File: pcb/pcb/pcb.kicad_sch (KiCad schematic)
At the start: 22 parts, among them J1 UART, J2 Barrel_Jack, J3 Stepper, SW1 RESET, SW2 FLASH, U1 ESP32-WROOM-32, U2 TSR_1-2433

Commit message: tweaks from reddit wiki
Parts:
- H1: footprint MountingHole:MountingHole_2.7mm_M2.5_Pad -> MountingHole:MountingHole_3.2mm_M3_DIN965_Pad
- H2, H3, H4: footprint MountingHole:MountingHole_2.5mm_Pad -> MountingHole:MountingHole_3.2mm_M3_DIN965_Pad
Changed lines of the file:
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@@
       (effects (font (size 1.27 1.27)) (justify left))
     )
-    (property "Footprint" "MountingHole:MountingHole_2.5mm_Pad" (id 2) (at 52.07 27.94 0)
+    (property "Footprint" "MountingHole:MountingHole_3.2mm_M3_DIN965_Pad" (id 2) (at 52.07 27.94 0)
       (effects (font (size 1.27 1.27)) hide)
     )
@@
       (effects (font (size 1.27 1.27)) (justify left))
     )
-    (property "Footprint" "MountingHole:MountingHole_2.7mm_M2.5_Pad" (id 2) (at 34.29 27.94 0)
+    (property "Footprint" "MountingHole:MountingHole_3.2mm_M3_DIN965_Pad" (id 2) (at 34.29 27.94 0)
       (effects (font (size 1.27 1.27)) hide)
     )
@@
       (effects (font (size 1.27 1.27)) (justify left))
     )
-    (property "Footprint" "MountingHole:MountingHole_2.5mm_Pad" (id 2) (at 69.85 27.94 0)
+    (property "Footprint" "MountingHole:MountingHole_3.2mm_M3_DIN965_Pad" (id 2) (at 69.85 27.94 0)
       (effects (font (size 1.27 1.27)) hide)
     )
@@
       (effects (font (size 1.27 1.27)) (justify left))
     )
-    (property "Footprint" "MountingHole:MountingHole_2.5mm_Pad" (id 2) (at 87.63 27.94 0)
+    (property "Footprint" "MountingHole:MountingHole_3.2mm_M3_DIN965_Pad" (id 2) (at 87.63 27.94 0)
       (effects (font (size 1.27 1.27)) hide)
     )
@@
     )
     (path "/34fa3d54-c535-425c-b022-e1943d8d5f86"
-      (reference "H1") (unit 1) (value "MountingHole") (footprint "MountingHole:MountingHole_2.7mm_M2.5_Pad")
+      (reference "H1") (unit 1) (value "MountingHole") (footprint "MountingHole:MountingHole_3.2mm_M3_DIN965_Pad")
     )
     (path "/00d9b647-6f7b-4061-b8f8-f07282eb45d6"
-      (reference "H2") (unit 1) (value "MountingHole") (footprint "MountingHole:MountingHole_2.5mm_Pad")
+      (reference "H2") (unit 1) (value "MountingHole") (footprint "MountingHole:MountingHole_3.2mm_M3_DIN965_Pad")
     )
     (path "/72d1a3aa-0e7b-4b10-a84c-7a0d93e80db5"
-      (reference "H3") (unit 1) (value "MountingHole") (footprint "MountingHole:MountingHole_2.5mm_Pad")
+      (reference "H3") (unit 1) (value "MountingHole") (footprint "MountingHole:MountingHole_3.2mm_M3_DIN965_Pad")
     )
     (path "/b3ffd185-6873-4234-b901-27672efba3ad"
-      (reference "H4") (unit 1) (value "MountingHole") (footprint "MountingHole:MountingHole_2.5mm_Pad")
+      (reference "H4") (unit 1) (value "MountingHole") (footprint "MountingHole:MountingHole_3.2mm_M3_DIN965_Pad")
     )
     (path "/f859e7d0-40bd-4ce3-9e1e-50d116474f0f"

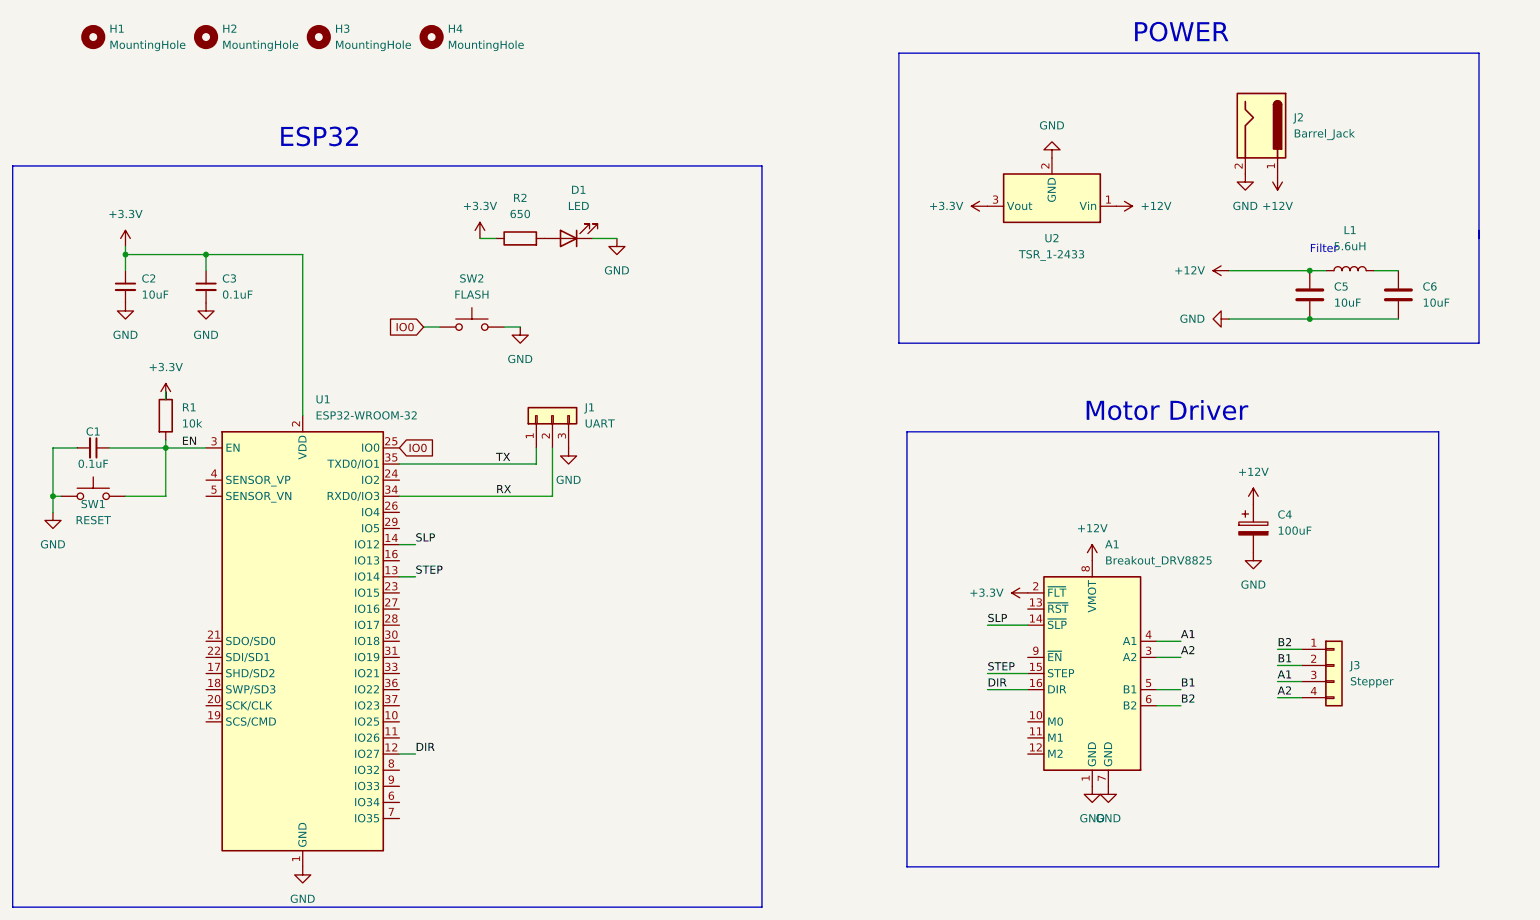
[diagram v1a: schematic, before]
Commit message: add activity led and general tidy
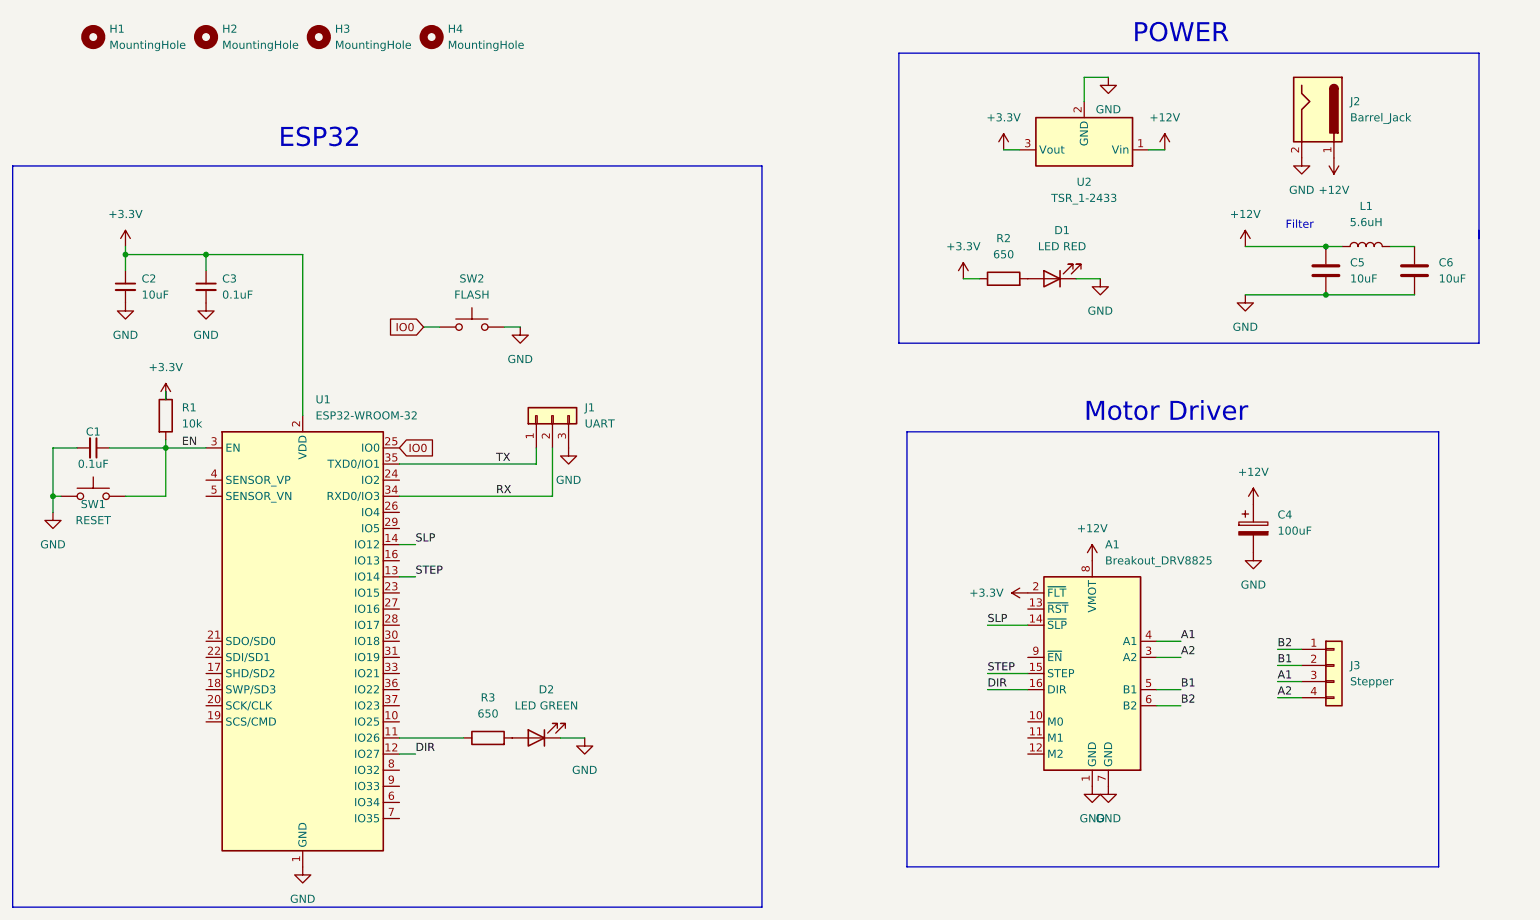
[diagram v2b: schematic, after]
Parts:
- added D2: LED GREEN, LED_SMD:LED_1206_3216Metric_Pad1.42x1.75mm_HandSolder, symbol Device:LED
- added R3: 650, Resistor_SMD:R_1206_3216Metric_Pad1.30x1.75mm_HandSolder, symbol Device:R
- D1: value LED -> LED RED
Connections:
- net GND: now also D2.1 (K)
- net at U1.11 (IO26): now also R3.1
- new net: D2.2 (A), R3.2
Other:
- moved on the sheet: C5, C6, D1, J2, L1, R2, U2

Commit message: general tweaks
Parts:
- H1, H2, H3, H4: footprint MountingHole:MountingHole_3.2mm_M3_DIN965_Pad -> MountingHole:MountingHole_3.2mm_M3_Pad
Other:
- title: (none) -> twilight
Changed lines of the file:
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@@
 (kicad_sch (version 20211123) (generator eeschema)
   (paper "A4")
+  (title_block
+    (title "twilight")
+    (date "2022-01-28")
+    (rev "1.0")
+    (comment 4 "ESP32 and DRV8825 based stepper motor controller")
+  )
   (junction (at 52.07 62.23) (diameter 0) (color 0 0 0 0)
   )
@@
   )
   (wire (pts (xy 104.14 92.71) (xy 104.14 95.25))
+    (stroke (width 0) (type default) (color 0 0 0 0))
+  )
+  (wire (pts (xy 179.07 115.57) (xy 181.61 115.57))
     (stroke (width 0) (type default) (color 0 0 0 0))
   )
@@
       (effects (font (size 1.27 1.27)) (justify left))
     )
-    (property "Footprint" "MountingHole:MountingHole_3.2mm_M3_DIN965_Pad" (id 2) (at 52.07 27.94 0)
+    (property "Footprint" "MountingHole:MountingHole_3.2mm_M3_Pad" (id 2) (at 52.07 27.94 0)
       (effects (font (size 1.27 1.27)) hide)
     )
@@
       (effects (font (size 1.27 1.27)) (justify left))
     )
-    (property "Footprint" "MountingHole:MountingHole_3.2mm_M3_DIN965_Pad" (id 2) (at 34.29 27.94 0)
+    (property "Footprint" "MountingHole:MountingHole_3.2mm_M3_Pad" (id 2) (at 34.29 27.94 0)
       (effects (font (size 1.27 1.27)) hide)
     )
@@
       (effects (font (size 1.27 1.27)) (justify left))
     )
-    (property "Footprint" "MountingHole:MountingHole_3.2mm_M3_DIN965_Pad" (id 2) (at 69.85 27.94 0)
+    (property "Footprint" "MountingHole:MountingHole_3.2mm_M3_Pad" (id 2) (at 69.85 27.94 0)
       (effects (font (size 1.27 1.27)) hide)
     )
@@
       (effects (font (size 1.27 1.27)) (justify left))
     )
-    (property "Footprint" "MountingHole:MountingHole_3.2mm_M3_DIN965_Pad" (id 2) (at 87.63 27.94 0)
+    (property "Footprint" "MountingHole:MountingHole_3.2mm_M3_Pad" (id 2) (at 87.63 27.94 0)
       (effects (font (size 1.27 1.27)) hide)
     )
@@
     (pin "1")
   )
-  (symbol (lib_id "power:+3.3V") (at 181.61 115.57 90) (unit 1)
-    (in_bom yes) (on_board yes) (fields_autoplaced)
-    (property "Reference" "#PWR09" (id 0) (at 185.42 115.57 0)
-      (effects (font (size 1.27 1.27)) hide)
-    )
-    (property "Value" "+3.3V" (id 1) (at 177.8 115.5699 90)
-      (effects (font (size 1.27 1.27)) (justify left))
-    )
-    (property "Footprint" "" (id 2) (at 181.61 115.57 0)
-      (effects (font (size 1.27 1.27)) hide)
-    )
-    (property "Datasheet" "" (id 3) (at 181.61 115.57 0)
+  (symbol (lib_id "power:+3.3V") (at 179.07 115.57 0) (unit 1)
+    (in_bom yes) (on_board yes) (fields_autoplaced)
+    (property "Reference" "#PWR09" (id 0) (at 179.07 119.38 0)
+      (effects (font (size 1.27 1.27)) hide)
+    )
+    (property "Value" "+3.3V" (id 1) (at 179.07 110.49 0))
+    (property "Footprint" "" (id 2) (at 179.07 115.57 0)
+      (effects (font (size 1.27 1.27)) hide)
+    )
+    (property "Datasheet" "" (id 3) (at 179.07 115.57 0)
       (effects (font (size 1.27 1.27)) hide)
     )
@@
     )
     (path "/34fa3d54-c535-425c-b022-e1943d8d5f86"
-      (reference "H1") (unit 1) (value "MountingHole") (footprint "MountingHole:MountingHole_3.2mm_M3_DIN965_Pad")
+      (reference "H1") (unit 1) (value "MountingHole") (footprint "MountingHole:MountingHole_3.2mm_M3_Pad")
     )
     (path "/00d9b647-6f7b-4061-b8f8-f07282eb45d6"
-      (reference "H2") (unit 1) (value "MountingHole") (footprint "MountingHole:MountingHole_3.2mm_M3_DIN965_Pad")
+      (reference "H2") (unit 1) (value "MountingHole") (footprint "MountingHole:MountingHole_3.2mm_M3_Pad")
     )
     (path "/72d1a3aa-0e7b-4b10-a84c-7a0d93e80db5"
-      (reference "H3") (unit 1) (value "MountingHole") (footprint "MountingHole:MountingHole_3.2mm_M3_DIN965_Pad")
+      (reference "H3") (unit 1) (value "MountingHole") (footprint "MountingHole:MountingHole_3.2mm_M3_Pad")
     )
     (path "/b3ffd185-6873-4234-b901-27672efba3ad"
-      (reference "H4") (unit 1) (value "MountingHole") (footprint "MountingHole:MountingHole_3.2mm_M3_DIN965_Pad")
+      (reference "H4") (unit 1) (value "MountingHole") (footprint "MountingHole:MountingHole_3.2mm_M3_Pad")
     )
     (path "/f859e7d0-40bd-4ce3-9e1e-50d116474f0f"

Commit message: tidy schematic
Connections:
- net +12V: no longer U2.1 (Vin)
- net A1: now also J3.4 (Pin_4); no longer J3.3 (Pin_3)
- net A2: now also J3.3 (Pin_3); no longer J3.4 (Pin_4)
- net at C6.1, L1.2: now also U2.1 (Vin)
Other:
- moved on the sheet: C5, C6, D1, J2, J3, L1, R2, U2

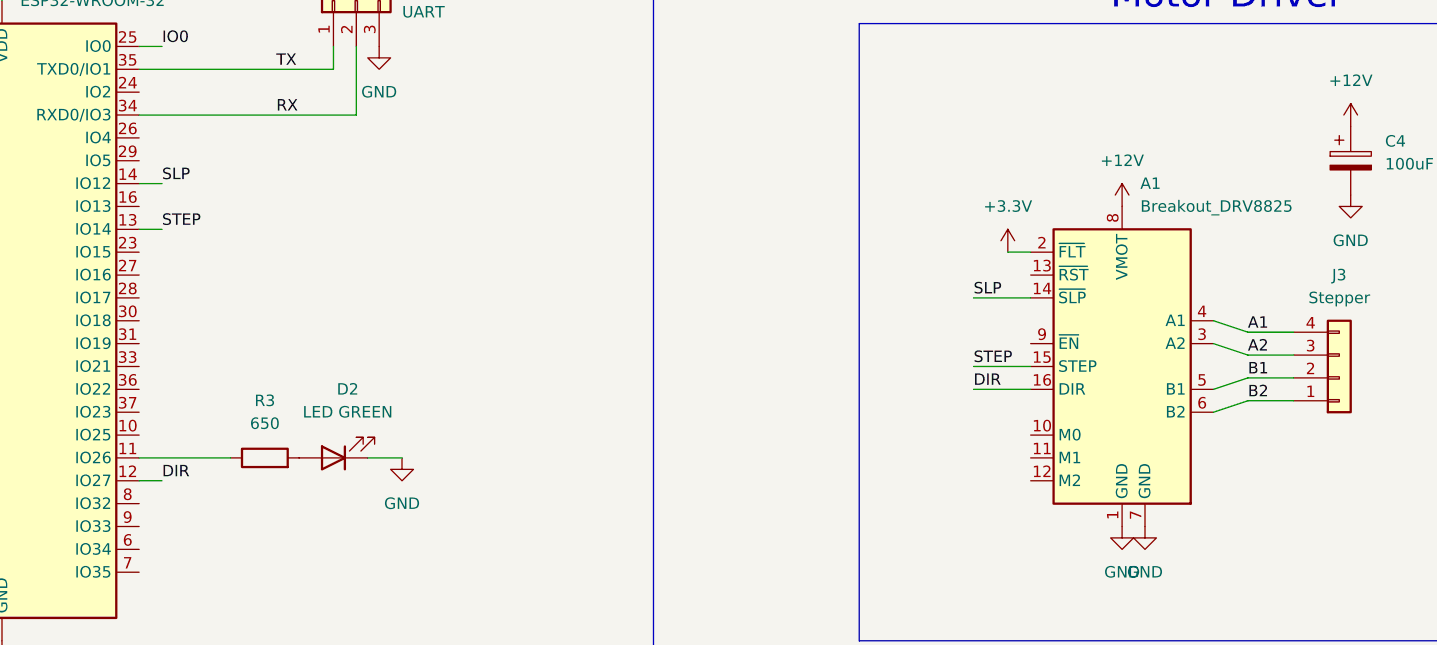
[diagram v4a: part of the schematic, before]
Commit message: Reroute pcb
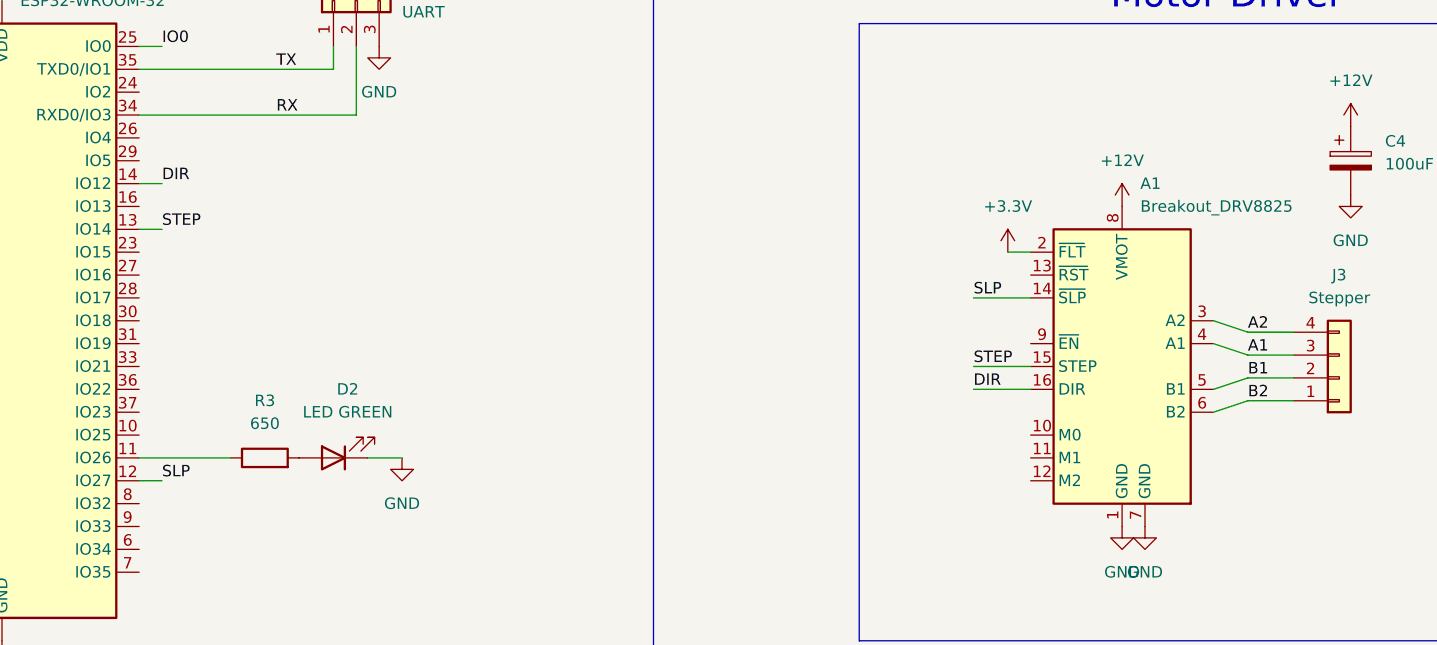
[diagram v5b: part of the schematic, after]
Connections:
- net A1: now also J3.3 (Pin_3); no longer J3.4 (Pin_4)
- net A2: now also J3.4 (Pin_4); no longer J3.3 (Pin_3)
- net DIR: now also U1.14 (IO12); no longer U1.12 (IO27)
- net SLP: now also U1.12 (IO27); no longer U1.14 (IO12)
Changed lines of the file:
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@@
     (effects (font (size 3 3)) (justify left bottom))
   )
-  (label "DIR" (at 85.09 140.97 0)
+  (label "SLP" (at 85.09 140.97 0)
     (effects (font (size 1.27 1.27)) (justify left bottom))
   )
@@
     (effects (font (size 1.27 1.27)) (justify left bottom))
   )
-  (label "SLP" (at 85.09 107.95 0)
+  (label "DIR" (at 85.09 107.95 0)
     (effects (font (size 1.27 1.27)) (justify left bottom))
   )
@@
     (effects (font (size 1.27 1.27)) (justify left bottom))
   )
-  (label "A1" (at 205.74 124.46 0)
+  (label "A2" (at 205.74 124.46 0)
     (effects (font (size 1.27 1.27)) (justify left bottom))
   )
@@
     (effects (font (size 1.27 1.27)) (justify left bottom))
   )
-  (label "A2" (at 205.74 127 0)
+  (label "A1" (at 205.74 127 0)
     (effects (font (size 1.27 1.27)) (justify left bottom))
   )
@@
   (symbol (lib_id "power:GND") (at 180.34 60.96 0) (unit 1)
     (in_bom yes) (on_board yes) (fields_autoplaced)
-    (property "Reference" "#PWR?" (id 0) (at 180.34 67.31 0)
+    (property "Reference" "#PWR0104" (id 0) (at 180.34 67.31 0)
       (effects (font (size 1.27 1.27)) hide)
     )
@@
   (symbol (lib_id "power:+12V") (at 180.34 45.72 0) (unit 1)
     (in_bom yes) (on_board yes) (fields_autoplaced)
-    (property "Reference" "#PWR?" (id 0) (at 180.34 49.53 0)
+    (property "Reference" "#PWR0102" (id 0) (at 180.34 49.53 0)
       (effects (font (size 1.27 1.27)) hide)
     )
@@
   (symbol (lib_id "power:+3.3V") (at 251.46 45.72 0) (unit 1)
     (in_bom yes) (on_board yes) (fields_autoplaced)
-    (property "Reference" "#PWR?" (id 0) (at 251.46 49.53 0)
+    (property "Reference" "#PWR0101" (id 0) (at 251.46 49.53 0)
       (effects (font (size 1.27 1.27)) hide)
     )
@@
   (symbol (lib_id "power:GND") (at 251.46 60.96 0) (unit 1)
     (in_bom yes) (on_board yes) (fields_autoplaced)
-    (property "Reference" "#PWR?" (id 0) (at 251.46 67.31 0)
+    (property "Reference" "#PWR0103" (id 0) (at 251.46 67.31 0)
       (effects (font (size 1.27 1.27)) hide)
     )
@@
       (reference "#PWR024") (unit 1) (value "GND") (footprint "")
     )
+    (path "/7761aae3-7bd6-49b5-8b8c-43a1be571c6c"
+      (reference "#PWR0101") (unit 1) (value "+3.3V") (footprint "")
+    )
+    (path "/715835ac-3e09-49c6-87bf-3987b18ca82f"
+      (reference "#PWR0102") (unit 1) (value "+12V") (footprint "")
+    )
+    (path "/79da6dea-b3f5-4ab9-921a-033fd614b38f"
+      (reference "#PWR0103") (unit 1) (value "GND") (footprint "")
+    )
     (path "/1a69b35e-63d2-44fd-bb08-62ee1616de96"
-      (reference "#PWR?") (unit 1) (value "GND") (footprint "")
-    )
-    (path "/715835ac-3e09-49c6-87bf-3987b18ca82f"
-      (reference "#PWR?") (unit 1) (value "+12V") (footprint "")
-    )
-    (path "/7761aae3-7bd6-49b5-8b8c-43a1be571c6c"
-      (reference "#PWR?") (unit 1) (value "+3.3V") (footprint "")
-    )
-    (path "/79da6dea-b3f5-4ab9-921a-033fd614b38f"
-      (reference "#PWR?") (unit 1) (value "GND") (footprint "")
+      (reference "#PWR0104") (unit 1) (value "GND") (footprint "")
     )
     (path "/b03e052e-fb2e-4d5e-ae41-d75f2a2ed3e5"
